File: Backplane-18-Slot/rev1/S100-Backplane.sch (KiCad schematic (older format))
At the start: 127 parts, among them IC1 7805, IC2 LM4250, K1 CONN_3, P1 CONN_3X2, P10 CONN_1, P11 CONN_1, P12 CONN_2, P13 CONN_1, P14 CONN_1, P15 CONN_1, P16 CONN_1, P17 CONN_1, P18 CONN_1, P19 XILINX CABLE2, P2 CONN_9, P3 CONN_1, P4 CONN_1, P6 CONN_1, P7 CONN_1, P8 CONN_1, P9 CONN_1, Q1 2N3906, Q10 ^^NPN-BC817-SOT323, Q11 ^^NPN-BC817-SOT323, Q12 ^^NPN-BC817-SOT323, Q2 2N3904, Q3 TIP29, Q4 TIP30, Q5 ^^NPN-BC817-SOT323, Q6 ^^NPN-BC817-SOT323, Q7 ^^NPN-BC817-SOT323, Q8 ^^NPN-BC817-SOT323, Q9 ^^NPN-BC817-SOT323, SW1 SW_PUSH, U1 S100, U10 S100, U100 S100-EX, U11 S100, U12 S100, U13 S100, U14 S100, U15 S100, U16 S100, U17 LM1086CS, U18 74LS245, U19 74LS245, U2 S100, U20 74LS245, U21 XC9572XL-VQ44, U22 MAX3002, U3 S100, U4 S100, U5 S100, U6 S100, U7 S100, U8 S100, U9 S100

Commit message: Backplane-18-Slot rev1: add logo and resistors; board 406x216 mm
Source: S100 Backplane ANTS_MOD/S100 Backplane-001/BACKUPS/backup 04082013 1842/S100 Backplane-001
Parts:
- added R32, R34, R36, R38, R40, R42, R44: 10k, symbol R
- added R33, R35, R37, R39, R41, R43, R45: 100, symbol R
- added U1000: ^^LOGO1, symbol ^^LOGO1
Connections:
- wire segments 2146 -> 2183
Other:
- note removed: "Populate R20 if you want LED's ON"
- moved on the sheet: R20, R21

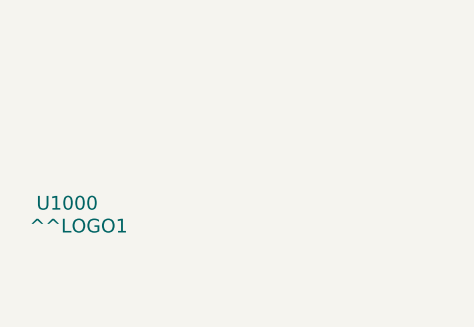
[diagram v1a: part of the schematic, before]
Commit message: Backplane-18-Slot rev1: add second logo; layout
Source: S100 Backplane ANTS_MOD/S100 Backplane-001/BACKUPS/backup 05082013 0041/S100 Backplane-001
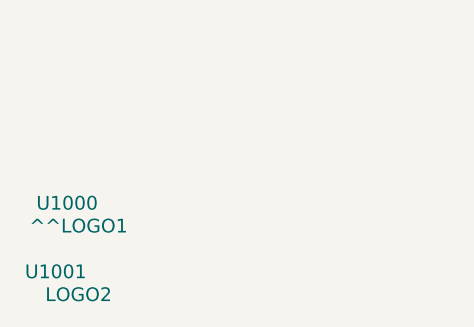
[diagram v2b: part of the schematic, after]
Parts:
- added U1001: LOGO2, symbol LOGO2
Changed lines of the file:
@@
 	10650 16550 10700 16550
 Connection ~ 10650 16450
+$Comp
+L LOGO2 U1001
+U 1 1 51FEAF52
+P 1550 32150
+F 0 "U1001" H 1550 32150 60  0000 C CNN
+F 1 "LOGO2" H 1650 32050 60  0000 C CNN
+F 2 "" H 1550 32150 60  0000 C CNN
+F 3 "" H 1550 32150 60  0000 C CNN
+	1    1550 32150
+	1    0    0    -1
+$EndComp
 $EndSCHEMATC

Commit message: Backplane-18-Slot rev1: add ATX PSU section and experimental logic (MSX slot, 27C801); RESET(s) jumper
Source: S100 Backplane ANTS_MOD/S100 Backplane-001/BACKUPS/backup 21082013 1727/S100 Backplane-001
From here to 20-10-2013 the schematic and board also hold the ATX PSU sub-board (refs 9xxx).
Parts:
- removed D1, D2, D3: LED, symbol LED
- removed F1, F2, F3: FUSE, symbol FUSE
- removed P1: CONN_3X2, symbol CONN_3X2
- removed P2: CONN_9, symbol CONN_9
- removed R17: 20K, symbol R
- removed R18: 470, symbol R
- removed U22: MAX3002, symbol MAX3002
- added C13, C2000, C2001, C2002, C2003, C2004, C2005, C2006, C9002, C9003: 0.1 uF, symbol C
- added C9000: 1uF, symbol CP1
- added C9001: 10uF, symbol CP1
- added D1: DIODE, symbol DIODE
- added D12, D2000, D2001, D2002, D2003, D9002, D9003: LED, symbol LED
- added D9000, D9001: 1N4148, symbol DIODE
- added P1: CONN_4, symbol CONN_4
- added P2: CPLD PINS, symbol CONN_12
- added P9000: ATX_POWER_24, ~, symbol ATX_POWER_24
- added P9001: ATX_POWER, symbol CONN_5
- added P9002: POWER_SW, symbol CONN_2
- added P9003, P9004, P9005, P9006: CONN_1, symbol CONN_1
- added P9007: SWITCH, symbol 3PDT
- added Q13, Q9001: 2N3904, symbol NPN
- added R2000, R2001, R2002, R2003, R47, R9000, R9002: 330, symbol R
- added R46: 1K, symbol R
- added R9001, R9003: 470, symbol R
- added R9004, R9005: 10k, symbol R
- added SW9000: POWER, symbol SW_PUSH
- added U2000: MSX_CART_SLOT, symbol MSX_CART_SLOT
- added U2001: 27C801, ~, symbol 27C801
- added U2002: 74LS670, ~, symbol 74LS670
- added U2003, U2004, U2005: 74LS245_B, ~, symbol 74LS245_B
- added U2006: 74LS02, ~, symbol 74LS02
- added U2007: 74LS04, ~, symbol 74LS04
- added U22, U24: 74LS125, symbol 74LS125
- added U23: 74LS14, symbol 74LS14
- added U9000: 74LS14PWR, ~, symbol 74LS14PWR
- added U9001: 74LS74PWR, ~, symbol 74LS74PWR
- K1: value CONN_3 -> RESET(s)
- R15: value 4700 -> 1K
- R16: value 20K -> 10K
- U18: footprint (none) -> ~
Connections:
- net labels added: +3.3V_B, +5V_B, -+12V, --12V, -12V_B, -A0, -A1, -A10, -A11, -A12, -A13, -A14, -A15, -A2, -A3, -A4, -A5, -A6, -A7, -A8, -A9, -CS1*, -CS12*, -CS2*, -D0, -D1, -D2, -D3, -D4, -D5, -D6, -D7, -GND, -MREQ*, -RD*, -SLTSL2*, -SOUNDIN, -SW1, -SW2, -VCC, -WR*, 12V, 5VSB, ATX_PWR_OK, CPLD_P36, CPLD_P37, CPLD_P38, GND_B, MAPER_A13, MAPER_A14, MAPER_A15, MAPER_A16, ~PS_ON
- net labels removed: F+16V, F+8V, F-16V
- wire segments 2183 -> 2601
- no-connect marks 2 -> 19
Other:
- note added: "ATX 24 Pin Supply Control Circuit & Plug"
- note added: "DIR: \nH = A to B\nL = B to A\n"
- note added: "LOGO(s)"
- note added: "MAX 128KB .ROM\nwith current mapper\n"Konami4""
- note added: "Since the size of the mapper is 8Kb, the memory banks are:\n\n Bank 1: 4000h - 5FFFh\n Bank 2: 6000h - 7FFFh\n Bank 3: 8000h - 9FFFh\n Bank 4: A000h - BFFFh\n\nAnd the address to change banks:\n\n Bank 1: <none>\n Bank 2: 6000h - 7FFFh (6000h used)\n Bank 3: 8000h - 9FFFh (8000h used)\n Bank 4: A000h - BFFFh (A000h used)"
- moved on the sheet: C10, C11, C12, C9, D10, D11, D4, D5, D6, D7, D8, D9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

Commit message: Backplane-18-Slot rev1: 18 slots; PIC18F2550 PSU control; XC6SLX9/FT232R experiments; first gerbers
Source: S100 Backplane ANTS_MOD/S100 Backplane-001/BACKUPS/backup 07102013 1647/S100 Backplane-001
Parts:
- removed C2000, C2001, C2002, C2003, C2004, C2005, C2006: 0.1 uF, symbol C
- removed C9000: 1uF, symbol CP1
- removed C9001: 10uF, symbol CP1
- removed D10, D11, D2000, D2001, D2002, D2003, D7, D8, D9: LED, symbol LED
- removed D9000, D9001: 1N4148, symbol DIODE
- removed P19: XILINX CABLE2, symbol CONN_5X2
- removed P2: CPLD PINS, symbol CONN_12
- removed P9007: SWITCH, symbol 3PDT
- removed Q10, Q11, Q12, Q6, Q7, Q8, Q9: ^^NPN-BC817-SOT323, symbol ^^NPN-BC817-SOT323
- removed R2000, R2001, R2002, R2003: 330, symbol R
- removed R32, R34, R36, R38, R40, R42, R44, R9005: 10k, symbol R
- removed R33, R35, R37, R39, R41, R43, R45: 100, symbol R
- removed R9003: 470, symbol R
- removed U17: LM1086CS, symbol LM1086CS
- removed U18: 74LS245, ~, symbol 74LS245
- removed U19, U20: 74LS245, symbol 74LS245
- removed U2000: MSX_CART_SLOT, symbol MSX_CART_SLOT
- removed U2001: 27C801, ~, symbol 27C801
- removed U2002: 74LS670, ~, symbol 74LS670
- removed U2003, U2004, U2005: 74LS245_B, ~, symbol 74LS245_B
- removed U2006: 74LS02, ~, symbol 74LS02
- removed U2007: 74LS04, ~, symbol 74LS04
- removed U21: XC9572XL-VQ44, symbol XC9572XL-VQ44
- removed U22, U24: 74LS125, symbol 74LS125
- removed U9000: 74LS14PWR, ~, symbol 74LS14PWR
- removed U9001: 74LS74PWR, ~, symbol 74LS74PWR
- added C14, C15, C16, C17, C18, C19, C20, C21, C22, C23, C24, C25, C26, C27: 0.1 uF, symbol C
- added C28, C29, C30, C31, C32, C33, C34, C35: 10 uF, symbol CP
- added D2, D3: LED, symbol LED
- added D4000: TX, symbol LED
- added D4001: RX, symbol LED
- added J4000: USB_2, symbol USB_2
- added J9002: ISP_M2, symbol RJ12
- added JP4, JP5, JP6: JUMPER, PIN_ARRAY_2X1, symbol JUMPER
- added K4000: I/O V?, ~, symbol CONN_3
- added P19: S100_MALE, S100_MALE, symbol S100_MALE
- added P2, P5: CONN_1, symbol CONN_1
- added P20: XILINX CABLE, symbol CONN_5X2
- added P21: CLK_CPU, symbol DIL14
- added P22: CPLD_JTAG, symbol CONN_2X2
- added P23: PF_JTAG, symbol CONN_2X2
- added P24: S6_JTAG, symbol CONN_2X2
- added P25: CLK_SEL, ~, symbol CONN_3X2
- added P26: PROG_B, symbol CONN_2
- added P27: CONN_6, symbol CONN_6
- added P4000: FT232R I/O, symbol CONN_10
- added Q9002: 2N3904, symbol NPN
- added R18, R4000, R4001: 330, symbol R
- added R9008: 10k, symbol R
- added R9009: 470, symbol R
- added SW2: PROG_B, symbol SW_PUSH
- added U17: S100, symbol S100_FEMALE
- added U18: 74LS541, symbol 74LS541
- added U19, U20, U21, U22, U24, U25: 74HC245, symbol 74HC245
- added U26, U27: 74LS244, ~, symbol 74LS244
- added U29: PAC_GHOST, symbol PAC_GHOST
- added U30: XC6SLX9-TQ144, symbol XC6SLX9-TQ144
- added U3000, U6001: SRAM_512KB, symbol SRAM_512KB
- added U3001: K6R4008C1D-SRAM_512KX8, ~, symbol K6R4008C1D-SRAM_512KX8
- added U31: 23LC1024, symbol 23LC1024
- added U32: XCF02S, symbol XCF02S
- added U33: CLK_FPGA1, symbol CRYSTAL_OSC_SMD
- added U34: LDO_REG_7805, ~, symbol LDO_REG_7805
- added U35: LM1086CS, symbol LM1086CS
- added U36: LF25CDT, symbol LF25CDT
- added U37: LD1117DT12, symbol LD1117DT12
- added U38, U39: POWER_SELECT, symbol POWER_SELECT
- added U40, U41, U43, U44: 74LS245, symbol 74LS245
- added U4000: FT232R, symbol FT232R
- added U42, U45: 74LVC245, ~, symbol 74LVC245
- added U6000: IS61LV5128AL-SOJ32, ~, symbol IS61LV5128AL-SOJ32
- added U9000: PIC18F2550, symbol PIC18F2550
- added U?: SMD1PAD, symbol SMD1PAD
- R19, R24, R29: value 0 -> 330
- R20, R25, R26: value 100 -> 330
- R21: value 10k -> 100
- R22, R23: value 0 -> 100
- R27: value 100 -> 10K; Digikey (none) -> ??
- R28, R30: value 0 -> 4K7
- R31: value 0 -> 1K
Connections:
- net labels added: +16V, +8V, -16V, /BUSAK, /BUSRQ, /HALT, /INT, /IORQ, /M1, /MREQ, /NMI, /RD, /RESET, /RFSH, /WAIT, /WR, 0V, 0V_A, 0V_B, 0V_C, 25LC_CS, 25LC_S0, 25LC_SCK, 25LC_SI, A0b, A10b, A11b, A12b, A13b, A14b, A15b, A16, A16b, A17, A17b, A18, A18b, A19, A19b, A1b, A20, A20b, A21, A21b, A22, A23, A2b, A3b, A4b, A5b, A6b, A7b, A8b, A9b, ADSB*, ATX_PWRUP, B_/RD, B_/WR, CDSB*, CLK, CLK_CPU, CLK_CPU2, CLOCK*, CPLD1_TDI, CPLD1_TDO, CPLD_1, CPLD_22, CPLD_23, CPLD_53, CPLD_65, CPLD_66, CPLD_67, CPLD_68, CPLD_70, CPLD_71, CPLD_72, CPLD_74, CPLD_75, CPLD_76, CPLD_81, CTS_TTL, D0, D1, D2, D3, D4, D5, D6, D7, DATA_DIR, DBUSIN_EN, DBUSOUT_EN, DI0b, DI1b, DI2b, DI3b, DI4b, DI5b, DI6b, DI7b, DO0b, DO1b, DO2b, DO3b, DO4b, DO5b, DO6b, DO7b, DODSB*, DSR_TTL, DTR_TTL, ERROR*, FPGA_10, FPGA_100, FPGA_101, FPGA_102, FPGA_104, FPGA_105, FPGA_11, FPGA_111, FPGA_112, FPGA_114, FPGA_115, FPGA_116, FPGA_117, FPGA_118, FPGA_119, FPGA_12, FPGA_120, FPGA_121, FPGA_123, FPGA_124, FPGA_126, FPGA_127, FPGA_131, FPGA_132, FPGA_133, FPGA_134, FPGA_137, FPGA_138, FPGA_139, FPGA_14, FPGA_140, FPGA_141, FPGA_142, FPGA_15, FPGA_16, FPGA_17, FPGA_2, FPGA_21, FPGA_22, FPGA_23, FPGA_24, FPGA_26, FPGA_27, FPGA_29, FPGA_30, FPGA_32, FPGA_33, FPGA_34, FPGA_35, FPGA_45, FPGA_46, FPGA_48, FPGA_5, FPGA_55, FPGA_56, FPGA_57, FPGA_58, FPGA_59, FPGA_6, FPGA_7, FPGA_78, FPGA_79, FPGA_8, FPGA_80, FPGA_81, FPGA_82, FPGA_83, FPGA_84, FPGA_87, FPGA_88, FPGA_9, FPGA_92, FPGA_93, FPGA_94, FPGA_95, FPGA_97, FPGA_98, FPGA_99, FPGA_CLK_0, FPGA_CLK_2, FT_VCCIO, HOLD*, INT*, IOREQb, M2_MCLR, M2_PGC, M2_PGD, M2_VDD, MAIN_VCC, NDEF1, NDEF2, NDEF3, NMI*, PF1_TDI, PF1_TDO, PHANTOM*, PHI, PHI_CLOCK, POC*, PWRFAIL*, RDY, RESET*, RFU1, RFU2, RFU3, RFU4, RTS_TTL, RX, S6LX9_TD0, S6LX9_TDI, SDSB*, SIN_TTL, SIXTN*, SLAVE_CLR*, SLAVE_CLR*vv, SOUT_TTL, SRAM3_A0, SRAM3_A1, SRAM3_A10, SRAM3_A11, SRAM3_A12, SRAM3_A13, SRAM3_A14, SRAM3_A15, SRAM3_A16, SRAM3_A17, SRAM3_A18, SRAM3_A2, SRAM3_A3, SRAM3_A4, SRAM3_A5, SRAM3_A6, SRAM3_A7, SRAM3_A8, SRAM3_A9, SRAM3_CS, SRAM3_D0, SRAM3_D1, SRAM3_D2, SRAM3_D3, SRAM3_D4, SRAM3_D5, SRAM3_D6, SRAM3_D7, SRAM3_OE, SRAM3_WE, SRAM_A0, SRAM_A1, SRAM_A10, SRAM_A11, SRAM_A12, SRAM_A13, SRAM_A14, SRAM_A15, SRAM_A16, SRAM_A17, SRAM_A18, SRAM_A2, SRAM_A3, SRAM_A4, SRAM_A5, SRAM_A6, SRAM_A7, SRAM_A8, SRAM_A9, SRAM_CS, SRAM_D0, SRAM_D1, SRAM_D2, SRAM_D3, SRAM_D4, SRAM_D5, SRAM_D6, SRAM_D7, SRAM_OE, SRAM_WE, TCK, TMA0*, TMA1*, TMA2*, TMA3*, TMS, TX, USB_VCC0, V1.2, V2.5, VCC_SRAM, VCC_SRAM3, VI0*, VI1*, VI2*, VI3*, VI4*, VI5*, VI6*, VI7*, pDBIN, pHLDA, pSTVAL*, pSYNC, pWR*, sHLTA, sINP, sINTA, sM1, sMEMR, sOUT, sWO*, sXTRQ*
- net labels removed: -+12V, --12V, -A0, -A1, -A10, -A11, -A12, -A13, -A14, -A15, -A2, -A3, -A4, -A5, -A6, -A7, -A8, -A9, -CS1*, -CS12*, -CS2*, -D0, -D1, -D2, -D3, -D4, -D5, -D6, -D7, -MREQ*, -RD*, -SLTSL2*, -SOUNDIN, -SW1, -SW2, -VCC, -WR*, A0_C, A10_C, A11_C, A12_C, A13_C, A14_C, A15_C, A1_C, A2_C, A3_C, A4_C, A5_C, A6_C, A7_C, A8_C, A9_C, CPLD2_TCK, CPLD2_TDI, CPLD2_TDO, CPLD2_TMS, CPLD_P26, CPLD_P27, CPLD_P28, CPLD_P29, CPLD_P30, CPLD_P31, CPLD_P32, CPLD_P33, CPLD_P36, CPLD_P37, CPLD_P38, MAPER_A13, MAPER_A14, MAPER_A15, MAPER_A16
- wire segments 2601 -> 3082
- no-connect marks 19 -> 69
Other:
- note added: "+3.3V from Power supply on Rail"
- note added: "+5V from Power supply on Rail"
- note added: "/WAIT is output from slave to Processor"
- note added: "2CCLK"
- note added: "ADDRESS INPUTS from S100 BUS"
- note added: "All routed to CPLD"
- note added: "B -> A"
- note added: "BANK 0"
- note added: "BANK 1"
- note added: "BANK 2"
- note added: "BANK 3"
- note added: "CONFIG"
- note added: "CPLD Pin 14"
- note added: "Connections for 25LC devices\n ---------------------------------------\n PICkit 2 Pin 25LC Device Pin (DIP)\n (1) VPP 1 nCS\n (2) Vdd 8 Vcc\n (3) GND 4 Vss\n (4) PGD 2 SO\n (5) PGC 6 SCK\n (6) AUX 5 SI\n 7 nHOLD - disabled (Vdd)\n 3 nWP - disabled (Vdd)"
- note added: "DATA I/O from/to S100 BUS"
- note added: "DATA RD/WR"
- note added: "DIN"
- note added: "DONE_LED"
- note added: "DPAK"
- note added: "INIT_B"
- note added: "INPUT"
- note added: "INPUT from S100 BUS"
- note added: "Input in terms of the Slave on the S100\nBus, DI is INPUT for salve, so, OUTPUT\nfor master"
- note added: "Jumper to exclude Program Flash 1 from Chain\njump 2->4, for inclusion jump 1->2 & 3->4"
- note added: "Jumper to exclude S3E 1 from Chain\njump 2->4, for inclusion jump 1->2 & 3->4"
- note added: "Jumper to exclude Uxx CPLD1 from Chain\njump 2->4, for inclusion jump 1->2 & 3->4"
- note added: "MASTER input"
- note added: "MODE Selector"
- note added: "OUTPUT"
- note added: "OUTPUT from Slave on S100 Bus,\nINPUT for the Master"
- note added: "OUTPUT to S100 BUS"
- note added: "PROG_B"
- note added: "Pin 1 => FT232R Transmit Asynchronous Data Output.\nPin 5 => FT232R Receiving Asynchronous Data Input."
- note added: "Pin 15 (Address line 18) S100 Bus"
- note added: "Pin 16 (Address line 16) S100 Bus"
- note added: "Pin 17 (Address line 17) S100 Bus"
- note added: "Pin 24 (Primary Processor clock line ) Input"
- note added: "Pin 44 (processor Instruction Fetch Cycle M1) Input"
- note added: "Pin 45 (I/O WR) Input"
- note added: "Pin 46 (I/O RD) Input"
- note added: "Pin 47 (MEM RD) Input"
- note added: "Pin 49 (clock line from another board) Input"
- note added: "Pin 5 (RXD) - INPUT\nPin 1 (TXD) - OUTPUT"
- note added: "Pin 54 (reset from another board) Input"
- note added: "Pin 59 (Address line 19) S100 Bus"
- note added: "Pin 61 (Address line 20) S100 Bus"
- note added: "Pin 62 (Address line 21) S100 Bus"
- note added: "Pin 63 (I/O REQUEST) Input"
- note added: "Pin 65 (MEM REQUEST) Input"
- note added: "Pin 68 (MEM WR) Input"
- note added: "Pin 72 (controld run/WAIT state of processor) Input"
- note added: "Pin 75 (forces processor to reset state) Input"
- note added: "Pin 77 (active low when processor write to I/O or MEM) Input"
- note added: "Pin 78 (active high when processor reads I/O or MEM) Input"
- note added: "Pin 79 (Address line 0) S100 Bus"
- note added: "Pin 97 (active low when processor is in Write status) Input"
- note added: "RX"
- note added: "SRAM SOJ to DIP"
- note added: "SRAM SOP to DIP"
- note added: "TO-220"
- note added: "TTL SERIAL to USB BREAKOUT"
- note added: "TX"
- note added: "Z80 DATA BUS INPUT to FPGA"
- note added: "Z80 DATA BUS OUTPUT from FPGA"
- note added: "Z80 INPUTS to FPGA"
- note added: "Z80 OUTPUTS from FPGA"
- note added: "from Pin 13 of CPLD"
- note added: "from Pin 18 of CPLD"
- note added: "~IORQ"
- note added: "~MREQ"
- note added: "~RD"
- note added: "~WR"
- note removed: "DIR: \nH = A to B\nL = B to A\n"
- note removed: "MAX 128KB .ROM\nwith current mapper\n"Konami4""
- note removed: "Pin 26"
- note removed: "Pin 45"
- note removed: "Pin 46"
- note removed: "Pin 47"
- note removed: "Pin 68"
- note removed: "Pin 73"
- note removed: "Since the size of the mapper is 8Kb, the memory banks are:\n\n Bank 1: 4000h - 5FFFh\n Bank 2: 6000h - 7FFFh\n Bank 3: 8000h - 9FFFh\n Bank 4: A000h - BFFFh\n\nAnd the address to change banks:\n\n Bank 1: <none>\n Bank 2: 6000h - 7FFFh (6000h used)\n Bank 3: 8000h - 9FFFh (8000h used)\n Bank 4: A000h - BFFFh (A000h used)"
- moved on the sheet: C9002, C9003, D9002, D9003, P9000, P9001, P9002, P9003, P9004, P9005, P9006, Q9001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

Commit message: Backplane-18-Slot rev1: drop SRAM/JTAG extras; 74LVC245 buffers
Source: S100 Backplane ANTS_MOD/S100 Backplane-001/BACKUPS/backup 07102013 2322/S100 Backplane-001
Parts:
- removed C16, C18, C20, C21, C24, C9: 0.1 uF, symbol C
- removed P2, P5: CONN_1, symbol CONN_1
- removed P22: CPLD_JTAG, symbol CONN_2X2
- removed P23: PF_JTAG, symbol CONN_2X2
- removed P24: S6_JTAG, symbol CONN_2X2
- removed P26: PROG_B, symbol CONN_2
- removed P27: CONN_6, symbol CONN_6
- removed U19, U20, U21, U22, U24: 74HC245, symbol 74HC245
- removed U26, U27: 74LS244, ~, symbol 74LS244
- removed U29: PAC_GHOST, symbol PAC_GHOST
- removed U3000, U6001: SRAM_512KB, symbol SRAM_512KB
- removed U3001: K6R4008C1D-SRAM_512KX8, ~, symbol K6R4008C1D-SRAM_512KX8
- removed U38, U39: POWER_SELECT, symbol POWER_SELECT
- removed U40, U41, U43, U44: 74LS245, symbol 74LS245
- removed U42: 74LVC245, ~, symbol 74LVC245
- removed U6000: IS61LV5128AL-SOJ32, ~, symbol IS61LV5128AL-SOJ32
- removed U?: SMD1PAD, symbol SMD1PAD
- added JP10, JP7, JP8, JP9: JUMPER, PIN_ARRAY_2X1, symbol JUMPER
- added U20, U21, U22, U24, U27: 74LVC245, ~, symbol 74LVC245
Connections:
- net labels added: +16Vi, +8Vi, -16Vi, 0V_Ai, 0V_Bi, 0V_Ci, 0Vi, A0bi, A0y, A10bi, A10y, A11bi, A11y, A12bi, A12y, A13bi, A13y, A14bi, A14y, A15bi, A15y, A16bi, A16y, A17bi, A17y, A18bi, A18y, A19bi, A19y, A1bi, A1y, A20bi, A20y, A21bi, A21y, A22bi, A22y, A23bi, A23y, A2bi, A2y, A3bi, A3y, A4bi, A4y, A5bi, A5y, A6bi, A6y, A7bi, A7y, A8bi, A8y, A9bi, A9y, ADSB*i, CDSB*i, CLOCK*i, DI0bi, DI1bi, DI2bi, DI3bi, DI4bi, DI5bi, DI6bi, DI7bi, DO0bi, DO1bi, DO2bi, DO3bi, DO4bi, DO5bi, DO6bi, DO7bi, DODSB*i, ERROR*i, HOLD*i, INT*i, IOREQbi, MWRTi, NDEF1i, NDEF2i, NDEF3i, NMI*i, PHANTOM*i, PHIi, POC*i, PWRFAIL*i, RDYi, RESET*i, RFU1i, RFU2i, RFU4i, SDSB*i, SIXTN*i, SLAVE_CLR*i, TMA0*i, TMA1*i, TMA2*i, TMA3*i, VI0*i, VI1*i, VI2*i, VI3*i, VI4*i, VI5*i, VI6*i, VI7*i, XRDYi, pDBINi, pHLDAi, pSTVAL*i, pSYNCi, pWR*i, sHLTAi, sINPi, sINTAi, sM1i, sMEMRi, sOUTi, sWO*i, sXTRQ*i
- net labels removed: +8V, /BUSAK, /BUSRQ, /HALT, /INT, /IORQ, /M1, /MREQ, /NMI, /RD, /RESET, /RFSH, /WAIT, /WR, 0V_A, 0V_B, 0V_C, A0b, A10b, A11b, A12b, A13b, A14b, A15b, A16b, A17b, A18b, A19b, A1b, A20b, A21b, A2b, A3b, A4b, A5b, A6b, A7b, A8b, A9b, ADSB*, B_/RD, B_/WR, CDSB*, CLK, CLOCK*, CPLD1_TDI, CPLD1_TDO, CPLD_1, CPLD_22, CPLD_23, CPLD_53, CPLD_65, CPLD_66, CPLD_67, CPLD_68, CPLD_70, CPLD_71, CPLD_72, CPLD_74, CPLD_75, CPLD_76, CPLD_81, DI0b, DI1b, DI2b, DI3b, DI4b, DI5b, DI6b, DI7b, DO0b, DO1b, DO2b, DO3b, DO4b, DO5b, DO6b, DO7b, DODSB*, ERROR*, HOLD*, INT*, IOREQb, NDEF1, NDEF2, NDEF3, NMI*, PHANTOM*, PHI, POC*, PWRFAIL*, RDY, RESET*, RFU1, RFU2, RFU4, SDSB*, SIXTN*, SLAVE_CLR*, SLAVE_CLR*vv, SRAM3_A0, SRAM3_A1, SRAM3_A10, SRAM3_A11, SRAM3_A12, SRAM3_A13, SRAM3_A14, SRAM3_A15, SRAM3_A16, SRAM3_A17, SRAM3_A18, SRAM3_A2, SRAM3_A3, SRAM3_A4, SRAM3_A5, SRAM3_A6, SRAM3_A7, SRAM3_A8, SRAM3_A9, SRAM3_CS, SRAM3_D0, SRAM3_D1, SRAM3_D2, SRAM3_D3, SRAM3_D4, SRAM3_D5, SRAM3_D6, SRAM3_D7, SRAM3_OE, SRAM3_WE, SRAM_A0, SRAM_A1, SRAM_A10, SRAM_A11, SRAM_A12, SRAM_A13, SRAM_A14, SRAM_A15, SRAM_A16, SRAM_A17, SRAM_A18, SRAM_A2, SRAM_A3, SRAM_A4, SRAM_A5, SRAM_A6, SRAM_A7, SRAM_A8, SRAM_A9, SRAM_CS, SRAM_D0, SRAM_D1, SRAM_D2, SRAM_D3, SRAM_D4, SRAM_D5, SRAM_D6, SRAM_D7, SRAM_OE, SRAM_WE, TMA0*, TMA1*, TMA2*, TMA3*, VCC_SRAM, VCC_SRAM3, VI0*, VI1*, VI2*, VI3*, VI4*, VI5*, VI6*, VI7*, pDBIN, pHLDA, pSTVAL*, pSYNC, pWR*, sHLTA, sINP, sINTA, sM1, sMEMR, sOUT, sWO*, sXTRQ*
- wire segments 3082 -> 2873
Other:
- note added: "INPUTS to FPGA"
- note removed: "Connections for 25LC devices\n ---------------------------------------\n PICkit 2 Pin 25LC Device Pin (DIP)\n (1) VPP 1 nCS\n (2) Vdd 8 Vcc\n (3) GND 4 Vss\n (4) PGD 2 SO\n (5) PGC 6 SCK\n (6) AUX 5 SI\n 7 nHOLD - disabled (Vdd)\n 3 nWP - disabled (Vdd)"
- note removed: "Jumper to exclude Uxx CPLD1 from Chain\njump 2->4, for inclusion jump 1->2 & 3->4"
- note removed: "SRAM SOJ to DIP"
- note removed: "SRAM SOP to DIP"
- note removed: "Z80 DATA BUS INPUT to FPGA"
- note removed: "Z80 DATA BUS OUTPUT from FPGA"
- note removed: "Z80 INPUTS to FPGA"
- note removed: "Z80 OUTPUTS from FPGA"
- moved on the sheet: C10, C11, C12, C14, C15, C17, C19, C22, C25, C26, C27, D2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

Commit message: Backplane-18-Slot rev1: layout
Source: S100 Backplane ANTS_MOD/S100 Backplane-001/BACKUPS/backup 08102013 0115/S100 Backplane-001
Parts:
- removed C12: 0.1 uF, symbol C
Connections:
- net labels added: CLK_TIMER
- net labels removed: A16, A17, A18, A19, A22, A23, CLK_CPU, CLK_CPU2, DATA_DIR
- wire segments 2873 -> 2878
- no-connect marks 69 -> 67
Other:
- note removed: "CPLD Pin 14"
- moved on the sheet: D4, D5, D6, R24, R25, R26
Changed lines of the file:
@@
 	-34900 6550 -32750 6550
 Wire Wire Line
-	-14850 20200 -14750 20200
-Connection ~ -14250 20200
+	-22150 9650 -22050 9650
+Connection ~ -21550 9650
 Wire Wire Line
-	-14250 20200 -14350 20200
-Connection ~ -14250 19900
+	-21550 9650 -21650 9650
+Connection ~ -21550 9350
 Wire Wire Line
-	-14250 19900 -14350 19900
+	-21550 9350 -21650 9350
 Wire Wire Line
 	-25650 8900 -25850 8900
@@
 	-20550 3300 -19450 3300
 Wire Wire Line
-	-16550 13300 -15850 13300
+	-16200 16600 -15500 16600
 Wire Wire Line
-	-16550 13200 -15850 13200
+	-16200 16500 -15500 16500
 Wire Wire Line
-	-16550 13000 -15850 13000
+	-16200 16300 -15500 16300
 Wire Wire Line
 	-16550 12800 -15850 12800
@@
 	-15850 12900 -16550 12900
 Wire Wire Line
-	-15850 13100 -16550 13100
+	-15500 16400 -16200 16400
 Wire Wire Line
 	-25750 6000 -25550 6000
@@
 	-25850 8800 -25650 8800
 Wire Wire Line
-	-14250 20800 -14350 20800
+	-21550 10250 -21650 10250
 Wire Wire Line
-	-14250 19650 -14250 20800
+	-21550 9100 -21550 10250
 Wire Wire Line
-	-14250 19650 -14200 19650
+	-21550 9100 -21500 9100
 Wire Wire Line
-	-14250 20500 -14350 20500
-Connection ~ -14250 20500
+	-21550 9950 -21650 9950
+Connection ~ -21550 9950
 Wire Wire Line
-	-14850 20500 -14750 20500
+	-22150 9950 -22050 9950
 Wire Wire Line
-	-14850 19900 -14750 19900
+	-22150 9350 -22050 9350
 Wire Wire Line
 	-32700 6650 -33650 6650
@@
 	-1   0    0    1
 $EndComp
-Text Label -14200 19650 0    60   ~ 0
+Text Label -21500 9100 0    60   ~ 0
 GND
 $Comp
 L LED D5
 U 1 1 525243E2
-P -14550 20200
-F 0 "D5" H -14550 20300 50  0000 C CNN
-F 1 "LED" H -14550 20100 50  0000 C CNN
-F 2 "" H -14550 20200 60  0001 C CNN
-F 3 "" H -14550 20200 60  0001 C CNN
-	1    -14550 20200
+P -21850 9650
+F 0 "D5" H -21850 9750 50  0000 C CNN
+F 1 "LED" H -21850 9550 50  0000 C CNN
+F 2 "" H -21850 9650 60  0001 C CNN
+F 3 "" H -21850 9650 60  0001 C CNN
+	1    -21850 9650
 	1    0    0    -1
 $EndComp
@@
 L R R25
 U 1 1 525243E8
-P -15100 20200
-F 0 "R25" V -15020 20200 50  0000 C CNN
-F 1 "330" V -15100 20200 50  0000 C CNN
-F 2 "" H -15100 20200 60  0001 C CNN
-F 3 "" H -15100 20200 60  0001 C CNN
-	1    -15100 20200
+P -22400 9650
+F 0 "R25" V -22320 9650 50  0000 C CNN
+F 1 "330" V -22400 9650 50  0000 C CNN
+F 2 "" H -22400 9650 60  0001 C CNN
+F 3 "" H -22400 9650 60  0001 C CNN
+	1    -22400 9650
 	0    -1   -1   0
 $EndComp
@@
 L R R24
 U 1 1 525243EE
-P -15100 19900
-F 0 "R24" V -15020 19900 50  0000 C CNN
-F 1 "330" V -15100 19900 50  0000 C CNN
-F 2 "" H -15100 19900 60  0001 C CNN
-F 3 "" H -15100 19900 60  0001 C CNN
-	1    -15100 19900
+P -22400 9350
+F 0 "R24" V -22320 9350 50  0000 C CNN
+F 1 "330" V -22400 9350 50  0000 C CNN
+F 2 "" H -22400 9350 60  0001 C CNN
+F 3 "" H -22400 9350 60  0001 C CNN
+	1    -22400 9350
 	0    -1   -1   0
 $EndComp
@@
 L LED D4
 U 1 1 525243F4
-P -14550 19900
-F 0 "D4" H -14550 20000 50  0000 C CNN
-F 1 "LED" H -14550 19800 50  0000 C CNN
-F 2 "" H -14550 19900 60  0001 C CNN
-F 3 "" H -14550 19900 60  0001 C CNN
-	1    -14550 19900
+P -21850 9350
+F 0 "D4" H -21850 9450 50  0000 C CNN
+F 1 "LED" H -21850 9250 50  0000 C CNN
+F 2 "" H -21850 9350 60  0001 C CNN
+F 3 "" H -21850 9350 60  0001 C CNN
+	1    -21850 9350
 	1    0    0    -1
 $EndComp
@@
 L LED D6
 U 1 1 525243FA
-P -14550 20500
-F 0 "D6" H -14550 20600 50  0000 C CNN
-F 1 "LED" H -14550 20400 50  0000 C CNN
-F 2 "" H -14550 20500 60  0001 C CNN
-F 3 "" H -14550 20500 60  0001 C CNN
-	1    -14550 20500
+P -21850 9950
+F 0 "D6" H -21850 10050 50  0000 C CNN
+F 1 "LED" H -21850 9850 50  0000 C CNN
+F 2 "" H -21850 9950 60  0001 C CNN
+F 3 "" H -21850 9950 60  0001 C CNN
+	1    -21850 9950
 	1    0    0    -1
 $EndComp
@@
 L R R26
 U 1 1 52524400
-P -15100 20500
-F 0 "R26" V -15020 20500 50  0000 C CNN
-F 1 "330" V -15100 20500 50  0000 C CNN
-F 2 "" H -15100 20500 60  0001 C CNN
-F 3 "" H -15100 20500 60  0001 C CNN
-	1    -15100 20500
+P -22400 9950
+F 0 "R26" V -22320 9950 50  0000 C CNN
+F 1 "330" V -22400 9950 50  0000 C CNN
+F 2 "" H -22400 9950 60  0001 C CNN
+F 3 "" H -22400 9950 60  0001 C CNN
+	1    -22400 9950
 	0    -1   -1   0
 $EndComp
@@
 Text Label -24800 10600 0    60   ~ 0
 FPGA_10
-Text Label -24800 10700 0    60   ~ 0
+Text Label -15750 16100 2    60   ~ 0
 FPGA_9
-Text Label -24800 10800 0    60   ~ 0
+Text Label -22800 9950 2    60   ~ 0
 FPGA_8
-Text Label -24800 10900 0    60   ~ 0
+Text Label -22800 9650 2    60   ~ 0
 FPGA_7
-Text Label -24800 11000 0    60   ~ 0
+Text Label -22800 9350 2    60   ~ 0
 FPGA_6
 Text Label -23050 11000 2    60   ~ 0
@@
 Text Label -16550 12900 0    60   ~ 0
 FPGA_93
-Text Label -16550 13000 0    60   ~ 0
+Text Label -16200 16300 0    60   ~ 0
 FPGA_92
-Text Label -16550 13100 0    60   ~ 0
+Text Label -16200 16400 0    60   ~ 0
 FPGA_88
-Text Label -16550 13200 0    60   ~ 0
+Text Label -16200 16500 0    60   ~ 0
 FPGA_87
-Text Label -16550 13300 0    60   ~ 0
+Text Label -16200 16600 0    60   ~ 0
 FPGA_84
 Text Label -16550 10550 0    60   ~ 0
@@
 $EndComp
 $Comp
-L C C12
-U 1 1 52524559
-P -33250 3900
-F 0 "C12" H -33200 4000 50  0000 L CNN
-F 1 "0.1 uF" H -33200 3800 50  0000 L CNN
-F 2 "" H -33250 3900 60  0001 C CNN
-F 3 "" H -33250 3900 60  0001 C CNN
-	1    -33250 3900
-	1    0    0    -1
-$EndComp
-$Comp
 L C C11
 U 1 1 5252455F
@@
 NoConn ~ -31950 -3850
 NoConn ~ -31950 -3750
-NoConn ~ -31950 -3650
 NoConn ~ -31950 -3550
 NoConn ~ -31950 -3450
 NoConn ~ -31250 -3450
 NoConn ~ -31250 -3550
-NoConn ~ -31250 -3650
 NoConn ~ -31250 -3750
 NoConn ~ -31250 -3850
@@
 Text Label -29500 7850 0    60   ~ 0
 V3.3
-Text Label -30150 -2400 0    60   ~ 0
-CLK_CPU
 $Comp
 L GND #PWR022
@@
 Wire Wire Line
 	-23450 -2000 -23450 -2100
-Text Label -29000 13050 0    60   ~ 0
+Text Label -29700 13600 0    60   ~ 0
 FPGA_CLK_0
 Text Label -32450 13400 0    60   ~ 0
@@
 Text Label -31600 -2200 2    60   ~ 0
 PHI_CLOCK
-Text Label -31600 -2300 2    60   ~ 0
-CLK_CPU2
 Wire Wire Line
-	-15350 20500 -15500 20500
+	-22650 9950 -22800 9950
 Wire Wire Line
-	-15350 20200 -15500 20200
+	-22650 9650 -22800 9650
 Wire Wire Line
-	-15350 19900 -15500 19900
+	-22650 9350 -22800 9350
 Wire Wire Line
 	-24600 -4450 -23550 -4450
@@
 	-31250 -3350 -31100 -3350
 Wire Wire Line
-	-31100 -3350 -31100 -2700
+	-31100 -3650 -31100 -2700
 Wire Wire Line
 	-31100 -2700 -31400 -2700
@@
 	-31400 -2400 -31150 -2400
 Wire Wire Line
-	-31150 -2300 -31600 -2300
-Wire Wire Line
 	-31600 -2200 -31150 -2200
-Text Label -12850 6000 0    60   ~ 0
-A10
-Text Label -12850 5500 0    60   ~ 0
-A5
-Text Label -12850 5400 0    60   ~ 0
-A4
-Text Label -12850 5300 0    60   ~ 0
-A3
-Text Label -12850 6500 0    60   ~ 0
-A15
-Text Label -12850 6200 0    60   ~ 0
-A12
-Text Label -12850 5900 0    60   ~ 0
-A9
-Text Label -12850 5000 0    60   ~ 0
-A0
-Text Label -12850 5100 0    60   ~ 0
-A1
-Text Label -12850 5200 0    60   ~ 0
-A2
-Text Label -12850 5600 0    60   ~ 0
-A6
-Text Label -12850 5700 0    60   ~ 0
-A7
-Text Label -12850 5800 0    60   ~ 0
-A8
-Text Label -12850 6300 0    60   ~ 0
-A13
-Text Label -12850 6400 0    60   ~ 0
-A14
-Text Label -12850 6100 0    60   ~ 0
-A11
-Text Label -12850 6800 0    60   ~ 0
-A18
-Text Label -12850 6700 0    60   ~ 0
-A17
-Text Label -12850 6600 0    60   ~ 0
-A16
-Text Label -12850 6900 0    60   ~ 0
-A19
 Text Notes -14150 4100 0    60   ~ 0
 B -> A
@@
 Text Notes -15150 8950 0    60   ~ 0
 B -> A
-Text Label -12850 3100 0    60   ~ 0
-D0
-Text Label -12850 3200 0    60   ~ 0
-D1
-Text Label -12850 3300 0    60   ~ 0
-D2
-Text Label -12850 3400 0    60   ~ 0
-D3
-Text Label -12850 3500 0    60   ~ 0
-D4
-Text Label -12850 3600 0    60   ~ 0
-D5
-Text Label -12850 3700 0    60   ~ 0
-D6
-Text Label -12850 3800 0    60   ~ 0
-D7
 Text Label -14050 3400 0    60   ~ 0
 A5y
@@
 Text Label -13900 17100 0    60   ~ 0
 GND
-Text Label -15850 16800 2    60   ~ 0
-DATA_DIR
-Text Notes -16300 16800 2    40   ~ 0
-CPLD Pin 14
 Text Notes -11600 12700 2    60   ~ 0
 ~WR
@@
 	-14200 13300 -14450 13300
 Wire Wire Line
-	-15500 16800 -15850 16800
-Wire Wire Line
 	-5400 10000 -5800 10000
 Wire Wire Line
@@
 Wire Wire Line
 	-14300 8350 -14050 8350
-Text Label -12850 7000 0    60   ~ 0
-A20
-Text Label -12850 7100 0    60   ~ 0
-A21
-Text Label -12850 7200 0    60   ~ 0
-A22
-Text Label -12850 7300 0    60   ~ 0
-A23
 Text Label -14850 4900 0    60   ~ 0
 V3.3
@@
 Text Label -19450 3900 0    60   ~ 0
 A7y
+Wire Wire Line
+	-15500 16100 -15750 16100
+Wire Wire Line
+	-31250 -3650 -31100 -3650
+Connection ~ -31100 -3350
+Wire Wire Line
+	-31950 -3650 -32100 -3650
+Wire Wire Line
+	-32100 -3650 -32100 -3350
+Wire Wire Line
+	-32100 -3350 -31950 -3350
+Text Label -16150 13300 2    60   ~ 0
+PHI_CLOCK
+Wire Wire Line
+	-15850 13300 -16150 13300
+Text Label -30150 -2400 0    60   ~ 0
+CLK_TIMER
+Text Label -29850 13600 2    60   ~ 0
+CLK_TIMER
+Wire Wire Line
+	-29700 13600 -29850 13600
 $EndSCHEMATC
